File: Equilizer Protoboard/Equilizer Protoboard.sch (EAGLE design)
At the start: 14 parts, among them U1 ARDUINOR3-BPLACE

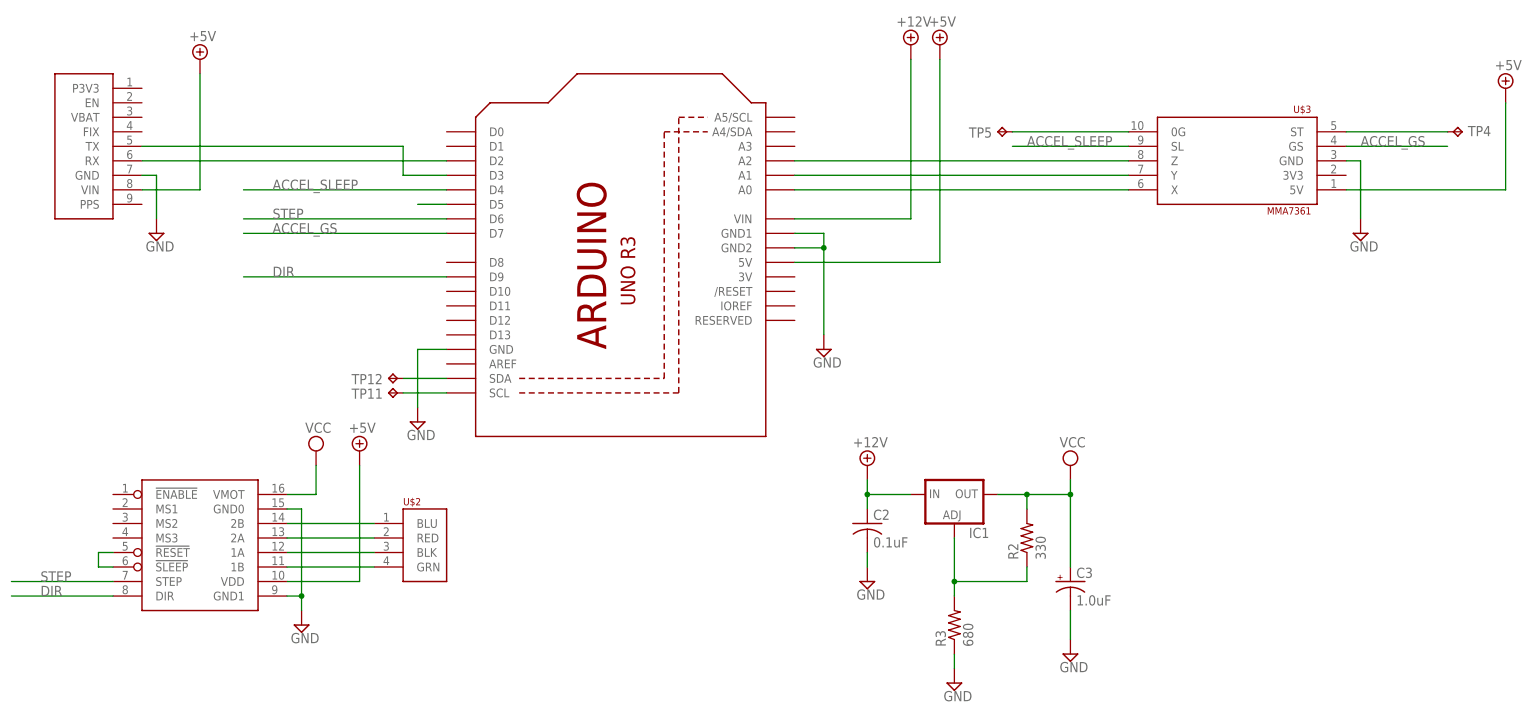
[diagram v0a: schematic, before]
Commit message: Added Datalog Parser
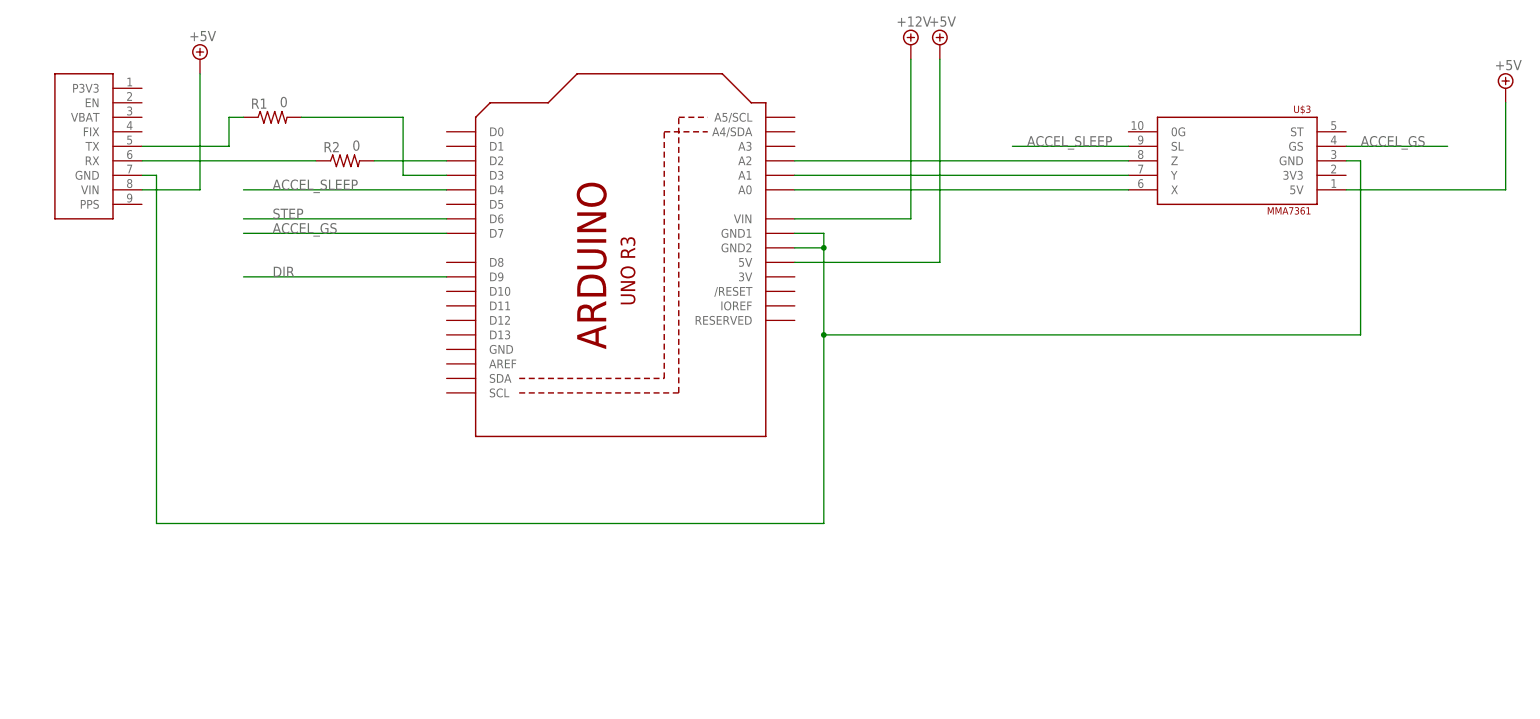
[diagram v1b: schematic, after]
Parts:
- removed C2: 0.1uF, adafruit:C-US050-025X075
- removed C3: 1.0uF, adafruit:CPOL-USE3.5-8
- removed IC1: (no value), v-reg:LM317TL
- removed R3: 680, adafruit:R-US_0207/7
- removed TP11, TP12, TP4, TP5: TPPAD1-13, testpad:TPPAD1-13
- removed U$1: A4988, custom:A4988
- removed U$2: POLOLU_STEPPER, custom:POLOLU_STEPPER
- added R1: 0, adafruit:R-US_0204/7
- R2: value 330 -> 0; device adafruit:R-US_0207/7 -> adafruit:R-US_0204/7
- U1: device custom:ARDUINOR3-BPLACE -> adafruit:ARDUINOR3-BPLACE
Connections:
- removed net GND: C2.2, C3.-, U$1.GND0, U$1.GND1, U$3.GND, U$4.GND, U1.GND, U1.GND1, U1.GND2
- removed net N$13: TP5.TP, U$3.0G
- removed net N$17: TP11.TP, U1.SCL
- removed net N$18: TP12.TP, U1.SDA
- removed net N$21: TP4.TP, U$3.ST
- removed net N$22: IC1.ADJ, R2.1, R3.2
- removed net N$29: U1.D5
- removed net N$6: U$1.1A, U$2.BLK
- removed net N$7: U$1.1B, U$2.GRN
- removed net VCC: C3.+, IC1.OUT, R2.2, U$1.VMOT
- net +12V: no longer C2.1, IC1.IN
- net +5V: no longer U$1.VDD
- net DIR: no longer U$1.DIR
- net N$1: now also U$3.GND, U$4.GND, U1.GND1, U1.GND2; no longer U$1.!RESET, U$1.!SLEEP
- net N$2: now also R2.1; no longer U1.D2
- net N$3: now also R1.1, U$4.TX; no longer U$1.2B, U$2.BLU
- net N$4: now also R1.2; no longer U$4.TX
- net N$5: now also R2.2, U1.D2; no longer U$1.2A, U$2.RED
- net STEP: no longer U$1.STEP
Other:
- moved on the sheet: R2
